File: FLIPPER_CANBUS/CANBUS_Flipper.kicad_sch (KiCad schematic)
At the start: 17 parts, among them J1 Conn_01x10_Socket, J2 Conn_01x08_Socket, J3 Conn_01x02, J4 Conn_01x02_Socket, U1 MCP2515-xST, U2 MAX3051, Y1 16 Mhz

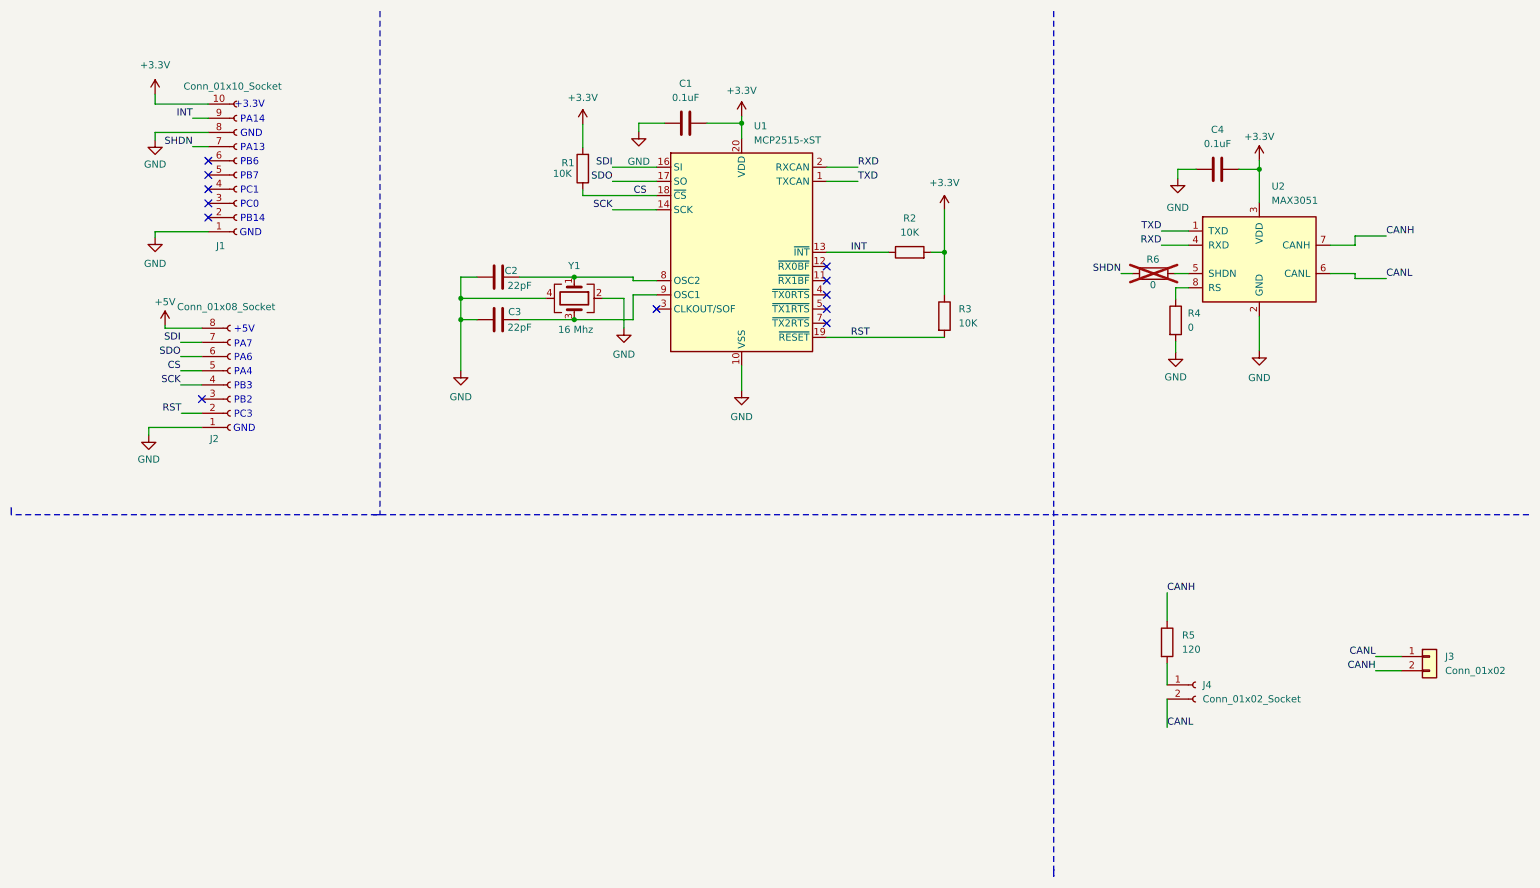
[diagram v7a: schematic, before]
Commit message: feat(Hw): change DNP for pre-manufacturing
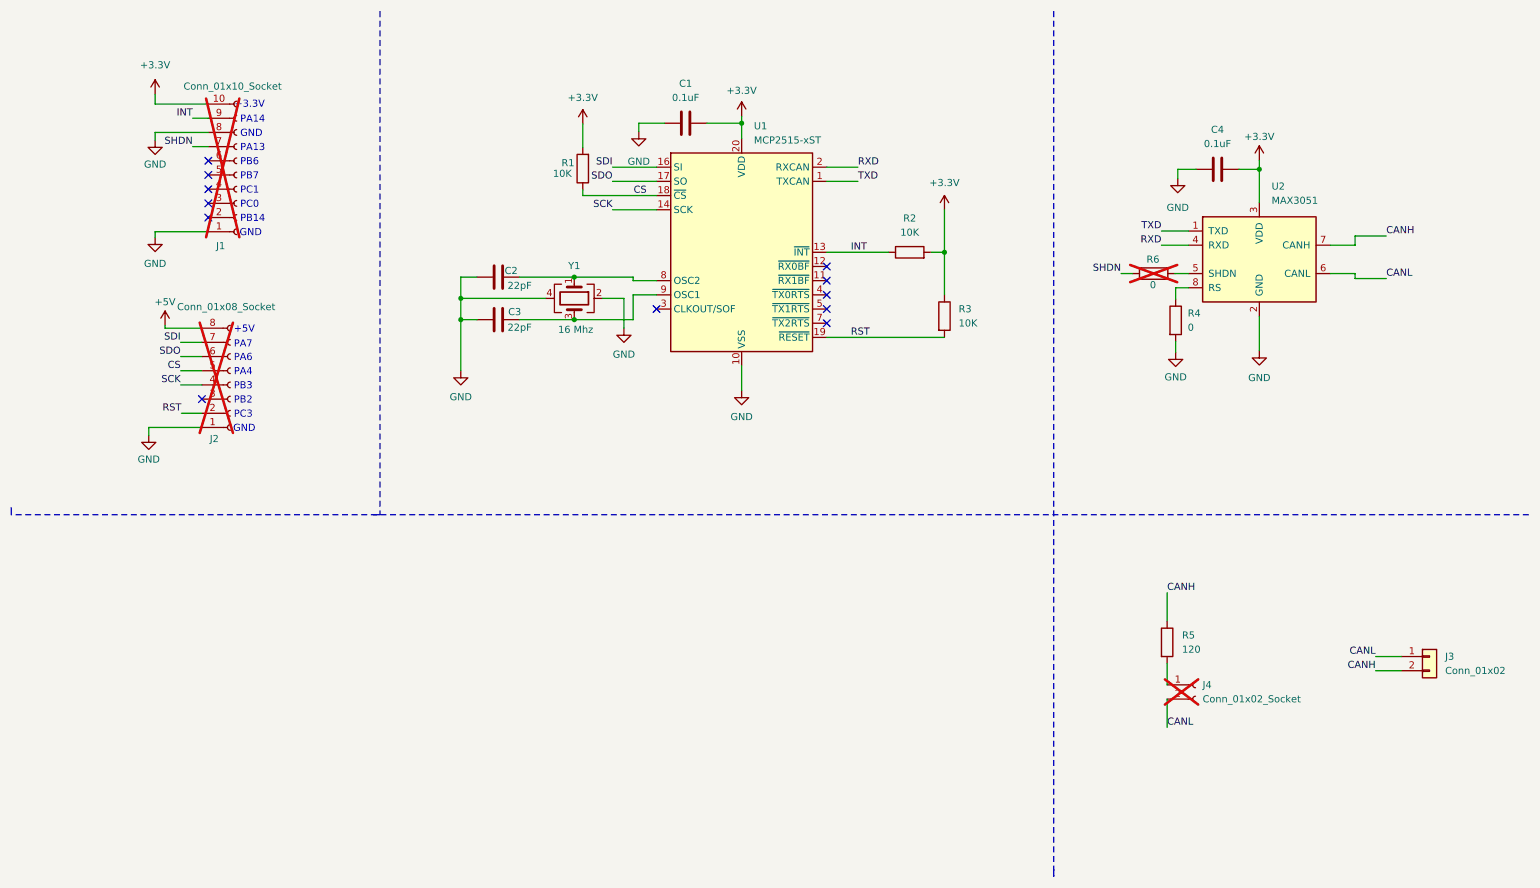
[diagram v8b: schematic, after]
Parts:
- J1, J2, J4: now not fitted
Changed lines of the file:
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@@
 		(in_bom yes)
 		(on_board yes)
-		(dnp no)
+		(dnp yes)
 		(fields_autoplaced yes)
 		(property "Reference" "J4"
@@
 		(in_bom yes)
 		(on_board yes)
-		(dnp no)
+		(dnp yes)
 		(property "Reference" "J1"
 			(at 49.403 53.467 0)
@@
 		(in_bom yes)
 		(on_board yes)
-		(dnp no)
+		(dnp yes)
 		(property "Reference" "J2"
 			(at 48.26 88.011 0)
